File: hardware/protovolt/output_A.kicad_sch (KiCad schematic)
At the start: 46 parts, among them Q1 BSC028N06LS3, Q3 BSC028N06LS3, Q4 BSC028N06LS3, Q5 BSC028N06LS3, Q6 BSC028N06LS3, U2 LM51772RHAR

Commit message: finish demo schematic
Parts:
- removed NT1: NetTie_2, symbol Device:NetTie_2
- added C11: 100n 100V, Resistor_SMD:R_0603_1608Metric, symbol Device:C
- added C14, C16: 100n, Capacitor_SMD:C_0603_1608Metric, symbol Device:C
- added C18, C23: 680p, Capacitor_SMD:C_0603_1608Metric, symbol Device:C
- added D1: 15V, Diode_SMD:D_SOD-123, symbol Device:D_Zener
- added J1, J2, J3, J4, J5, J6, J7, J8: Conn_01x03, Connector_PinHeader_2.54mm:PinHeader_1x03_P2.54mm_Vertical_SMD_Pin1Left, symbol Connector_Generic:Conn_01x03
- added J10, J9: Conn_02x03_Odd_Even, Connector_PinHeader_2.54mm:PinHeader_2x03_P2.54mm_Vertical_SMD, symbol Connector_Generic:Conn_02x03_Odd_Even
- added R10, R14: 10R, Resistor_SMD:R_0402_1005Metric, symbol Device:R
- added R11, R12, R8: 6.98k, Resistor_SMD:R_0402_1005Metric, symbol Device:R
- added R15, R16, R17, R18, R19, R20: 3R, Resistor_SMD:R_0402_1005Metric, symbol Device:R
- added R22, R7: 0R, Resistor_SMD:R_0402_1005Metric, symbol Device:R
- added R4: 100R, Resistor_SMD:R_0402_1005Metric, symbol Device:R
- added U1: INA226, Package_SO:VSSOP-10_3x3mm_P0.5mm, symbol Sensor_Energy:INA226
- C1: renamed from C22; value 10u -> 10u 100V; footprint (none) -> Capacitor_SMD:C_1210_3225Metric; LCSC (none) -> C5156756
- C10: renamed from C24; value 39u -> 39u 50V; footprint (none) -> Capacitor_SMD:CP_Elec_8x11.9; LCSC (none) -> C193240
- C12: renamed from C6; value 0.1u -> 100n 100V; footprint (none) -> Resistor_SMD:R_0603_1608Metric; LCSC (none) -> C88219
- C13: renamed from C5; value 100n -> 100n 100V; footprint (none) -> Resistor_SMD:R_0603_1608Metric; LCSC (none) -> C88219
- C15: renamed from C3; footprint (none) -> Capacitor_SMD:C_0603_1608Metric; LCSC (none) -> C30926
- C17: renamed from C20; footprint (none) -> Capacitor_SMD:C_0603_1608Metric; LCSC (none) -> C30926
- C19: renamed from C18; footprint (none) -> Capacitor_SMD:C_0603_1608Metric; LCSC (none) -> C84419
- C2: renamed from C7; value 10u -> 10u 100V; footprint (none) -> Capacitor_SMD:C_1210_3225Metric; LCSC (none) -> C5156756
- C20: renamed from C19; footprint (none) -> Capacitor_SMD:C_0603_1608Metric; LCSC (none) -> C84419
- C21: renamed from C1; value 0.1u -> 100n 100V; footprint (none) -> Resistor_SMD:R_0603_1608Metric; LCSC (none) -> C88219
- C22: renamed from C21; footprint (none) -> Capacitor_SMD:C_0603_1608Metric; LCSC (none) -> C30926
- C24: renamed from C4; footprint (none) -> Capacitor_SMD:C_0402_1005Metric; LCSC (none) -> C440165
- C25: renamed from C2; footprint (none) -> Capacitor_SMD:C_0402_1005Metric; LCSC (none) -> C1546
- C26: renamed from C13; footprint (none) -> Capacitor_SMD:C_0402_1005Metric; LCSC (none) -> C1572
- C27: renamed from C14; footprint (none) -> Capacitor_SMD:C_0402_1005Metric; LCSC (none) -> C354977
- C28: renamed from C15; footprint (none) -> Capacitor_SMD:C_0402_1005Metric; LCSC (none) -> C1567
- C29: renamed from C16; footprint (none) -> Capacitor_SMD:C_0402_1005Metric; LCSC (none) -> C82219
- C3: renamed from C9; value 10u -> 10u 100V; footprint (none) -> Capacitor_SMD:C_1210_3225Metric; LCSC (none) -> C5156756
- C4: renamed from C12; value 10u -> 10u 100V; footprint (none) -> Capacitor_SMD:C_1210_3225Metric; LCSC (none) -> C5156756
- C5: renamed from C23; value 10u -> 10u 100V; footprint (none) -> Capacitor_SMD:C_1210_3225Metric; LCSC (none) -> C5156756
- C6: renamed from C17; value 39u -> 39u 50V; footprint (none) -> Capacitor_SMD:CP_Elec_8x11.9; LCSC (none) -> C193240
- C7: renamed from C8; value 10u -> 10u 100V; footprint (none) -> Capacitor_SMD:C_1210_3225Metric; LCSC (none) -> C5156756
- C8: renamed from C11; value 10u -> 10u 100V; footprint (none) -> Capacitor_SMD:C_1210_3225Metric; LCSC (none) -> C5156756
- C9: renamed from C10; value 39u -> 39u 50V; footprint (none) -> Capacitor_SMD:CP_Elec_8x11.9; LCSC (none) -> C193240
- L1: footprint (none) -> Inductor_SMD:L_Changjiang_FXL1050; LCSC C149528 -> C5359259
- Q1: renamed from Q6; value BSC028N06LS3 -> BSC0702LS; LCSC C534316 -> C501503
- Q2: renamed from Q1; value BSC028N06LS3 -> BSC0702LS; LCSC C534316 -> C501503
- Q3: renamed from Q4; value BSC028N06LS3 -> BSC0702LS; LCSC C534316 -> C501503
- Q4: renamed from Q3; value BSC028N06LS3 -> BSC0702LS; LCSC C534316 -> C501503
- Q5: value BSC028N06LS3 -> BSC0702LS; LCSC C534316 -> C501503
- R1: renamed from R4; value R -> 0.010R; footprint (none) -> Resistor_SMD:R_2512_6332Metric; LCSC (none) -> C393070
- R13: renamed from R8; footprint (none) -> Resistor_SMD:R_0402_1005Metric; LCSC (none) -> C21376
- R2: footprint (none) -> Resistor_SMD:R_0402_1005Metric; LCSC (none) -> C286566
- R21: renamed from R9; footprint (none) -> Resistor_SMD:R_0402_1005Metric; LCSC (none) -> C25139
- R23: renamed from R10; footprint (none) -> Resistor_SMD:R_0402_1005Metric; LCSC (none) -> C25139
- R24: renamed from R11; footprint (none) -> Resistor_SMD:R_0402_1005Metric; LCSC (none) -> C47500
- R25: renamed from R16; footprint (none) -> Resistor_SMD:R_0402_1005Metric; LCSC (none) -> C25893
- R26: renamed from R20; value 20.5k -> 2.7k; footprint (none) -> Resistor_SMD:R_0402_1005Metric; LCSC (none) -> C25885
- R27: renamed from R21; footprint (none) -> Resistor_SMD:R_0402_1005Metric; LCSC (none) -> C21376
- R28: renamed from R22; value 33k -> 30.9k; footprint (none) -> Resistor_SMD:R_0402_1005Metric; LCSC C25555 -> C310222
- R3: renamed from R1; footprint (none) -> Resistor_SMD:R_2512_6332Metric; LCSC (none) -> C5375459
- R5: renamed from R3; value 511R -> 30.9k; footprint (none) -> Resistor_SMD:R_0402_1005Metric; LCSC (none) -> C310222
- R6: value 100k -> 0R; footprint (none) -> Resistor_SMD:R_0402_1005Metric; LCSC (none) -> C21376
- R9: renamed from R7; footprint (none) -> Resistor_SMD:R_0402_1005Metric; LCSC (none) -> C21376
- U2: LCSC (none) -> C41383743
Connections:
- net CSA: now also C18.1
- net DRV: now also R4.2; no longer Q1.4 (G)
- net GND: now also C12.1, C13.2, C19.2, C21.1, C25.2, C26.2, C27.2, C28.2, C29.2, R25.2, R26.2, R27.2, R28.2, U2.17 (AGND), U2.41 (GND), C11.1, C14.2, J10.1 (Pin_1), J10.3 (Pin_3), J10.5 (Pin_5), J3.3 (Pin_3), J5.3 (Pin_3), J6.3 (Pin_3), J7.3 (Pin_3), J8.3 (Pin_3), J9.2 (Pin_2), J9.4 (Pin_4), J9.6 (Pin_6), R16.2, R19.2, R7.1, U1.7 (GND)
- net HO1: now also R15.2; no longer U2.24 (HO1)
- net HO2: now also R18.2; no longer U2.32 (HO2)
- net ISNSN: now also R14.2
- net ISNSP: now also R10.2
- net LO1: now also R17.2; no longer U2.27 (LO1)
- net LO2: now also R20.2; no longer U2.30 (LO2)
- net SW2: now also C23.1
- net VBUS: now reaches C1.1, C12.2, C6.1, Q2.5 (D), R2.1, U2.36 (VIN)
- net VBUS: now also J10.2 (Pin_2), J10.4 (Pin_4), J10.6 (Pin_6), J2.1 (Pin_1), J8.1 (Pin_1)
- net at R6.2: now also U2.14 (FB/INT); no longer U2.11 (FLT)
- net VCC2: now reaches C20.1, R6.1, U2.29 (VCC2)
- net VCC2: now also J3.1 (Pin_1), J5.1 (Pin_1); no longer U2.14 (FB/INT), U2.7 (MODE)
- net ATRK: now reaches C29.1, U2.2 (SS/ATRK)
- net ATRK: now also J7.2 (Pin_2)
- net SYNC: now reaches U2.3 (SYNC)
- net SYNC: now also J5.2 (Pin_2)
- net at R2.2, R5.1, U2.37 (EN/UVLO): now also C11.2
- net RST: now reaches U2.38 (RST)
- net RST: now also J8.2 (Pin_2)
- net DTRK: now reaches U2.4 (DTRK)
- net DTRK: now also J7.1 (Pin_1)
- net BIAS: now reaches C21.2, U2.40 (BIAS)
- net BIAS: now also J2.2 (Pin_2), R22.1
- net SDA: now reaches U2.5 (CFG3(SDA))
- net SDA: now also J6.2 (Pin_2)
- net SCL: now reaches U2.6 (CFG4(SCL))
- net SCL: now also J6.1 (Pin_1)
- net at C10.1, C5.1, Q1.1 (S)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: now also D1.2 (A), J9.1 (Pin_1), J9.3 (Pin_3), J9.5 (Pin_5), U1.8 (Vbus)
- removed net GNDA: C12.1, C13.2, C19.2, C21.1, C25.2, C26.2, C27.2, C28.2, C29.2, R25.2, R26.2, R27.2, R28.2, U2.15 (VIN-FB), U2.17 (AGND), U2.41 (GND)
- new net: J4.2 (Pin_2), R11.2, U1.5 (SCL)
- new net: J4.1 (Pin_1), R12.2, U1.3 (~{Alert})
- new net: C16.1, R10.1, U1.10 (Vin+)
- new net: C16.2, R14.1, U1.9 (Vin-)
- new net: D1.1 (K), Q1.4 (G), R4.1
- new net: R15.1, U2.24 (HO1)
- new net: R7.2, U2.15 (VIN-FB)
- new net: R17.1, U2.27 (LO1)
- new net: R20.1, U2.30 (LO2)
- new net: R18.1, U2.32 (HO2)
- new net: C23.2, R19.1
- new net: J1.1 (Pin_1), U1.2 (A0)
- new net: J1.2 (Pin_2), U1.1 (A1)
- new net: C18.2, R16.1
- new net: J4.3 (Pin_3), R8.2, U1.4 (SDA)
- new net +3V3: C14.1, J1.3 (Pin_3), R11.1, R12.1, R8.1, U1.6 (VS)
- new net FLT: R22.2, U2.11 (FLT)
- new net MODE: J3.2 (Pin_2), U2.7 (MODE)
- no-connect marks 0 -> 1
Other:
- note added: "+5V: PWM/CCM GND: SLEEP"
- note added: "BSC0702LS 60V 84A 83W 2.7mΩ@10V,50A 2.3V 1 N-channel TDSON-8-EP(5x6) MOSFETs ROHS BSC028N06LS3 60V 100A 2.8mΩ@10V,50A 139W 2.2V 1 N-channel TDSON-8(5.2x5.9) MOSFETs ROHS"
- note added: "RT to GND I2C ADDR 0x6A RT to VCC2 I2C ADDR 0x6B"
- note added: "SOFT START 4.7ms"
- note added: "UVLO - RISING 4.28V - FALLING 4.11V"
- moved on the sheet: C15, C17, C22, C24, Q1, R13, R21, R23, R9

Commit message: route h-bridge
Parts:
- R22: value 0R -> 6.98k
- R3: LCSC C5375459 -> C20539438
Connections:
- net BIAS: no longer R22.1
- net VCC2: now also R22.1
- net ISNS_N: now reaches C15.1, R13.1, U2.19 (ISNSN)
- net ISNS_P: now reaches C15.2, R9.1, U2.20 (ISNSP)
- net CS_N: now reaches C24.2, R23.1, U2.21 (CSB)
- net CS_P: now reaches C24.1, R21.1, U2.22 (CSA)
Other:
- note added: "BSC0702LS 60V 84A 83W 2.7mΩ@10V,50A 2.3V 1 N-channel TDSON-8-EP(5x6) MOSFETs ROHS BSC028N06LS3 60V 100A 2.8mΩ@10V,50A 139W 2.2V 1 N-channel TDSON-8(5.2x5.9) MOSFETs ROHS IAUC60N04S6L030HATMA HALF-BRIDGE"
- note removed: "BSC0702LS 60V 84A 83W 2.7mΩ@10V,50A 2.3V 1 N-channel TDSON-8-EP(5x6) MOSFETs ROHS BSC028N06LS3 60V 100A 2.8mΩ@10V,50A 139W 2.2V 1 N-channel TDSON-8(5.2x5.9) MOSFETs ROHS"
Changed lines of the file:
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@@
 	)
 	(junction
+		(at 129.54 163.83)
+		(diameter 0)
+		(color 0 0 0 0)
+	)
+	(junction
 		(at 212.09 173.99)
 		(diameter 0)
@@
 	)
 	(junction
-		(at 129.54 168.91)
-		(diameter 0)
-		(color 0 0 0 0)
-	)
-	(junction
 		(at 152.4 163.83)
 		(diameter 0)
@@
 	(wire
 		(pts
-			(xy 129.54 168.91) (xy 154.94 168.91)
+			(xy 110.49 168.91) (xy 154.94 168.91)
 		)
 		(stroke
@@
 	(wire
 		(pts
-			(xy 105.41 163.83) (xy 152.4 163.83)
+			(xy 105.41 163.83) (xy 129.54 163.83)
 		)
 		(stroke
@@
 	(wire
 		(pts
+			(xy 129.54 163.83) (xy 152.4 163.83)
+		)
+		(stroke
+			(width 0)
+			(type default)
+		)
+	)
+	(wire
+		(pts
 			(xy 195.58 176.53) (xy 200.66 176.53)
 		)
@@
 	(wire
 		(pts
-			(xy 129.54 195.58) (xy 129.54 168.91)
-		)
-		(stroke
-			(width 0)
-			(type default)
-		)
-	)
-	(wire
-		(pts
 			(xy 144.78 203.2) (xy 154.94 203.2)
 		)
@@
 	(wire
 		(pts
+			(xy 129.54 163.83) (xy 129.54 195.58)
+		)
+		(stroke
+			(width 0)
+			(type default)
+		)
+	)
+	(wire
+		(pts
 			(xy 320.04 151.13) (xy 322.58 151.13)
 		)
@@
 		)
 	)
-	(wire
-		(pts
-			(xy 110.49 168.91) (xy 129.54 168.91)
-		)
-		(stroke
-			(width 0)
-			(type default)
-		)
-	)
 	(text "UVLO\n- RISING 4.28V\n- FALLING 4.11V"
 		(exclude_from_sim no)
@@
 		)
 	)
-	(text "BSC0702LS\n60V 84A 83W 2.7mΩ@10V,50A 2.3V 1 N-channel TDSON-8-EP(5x6) MOSFETs ROHS\n\nBSC028N06LS3\n60V 100A 2.8mΩ@10V,50A 139W 2.2V 1 N-channel TDSON-8(5.2x5.9) MOSFETs ROHS\n"
+	(text "BSC0702LS\n60V 84A 83W 2.7mΩ@10V,50A 2.3V 1 N-channel TDSON-8-EP(5x6) MOSFETs ROHS\n\nBSC028N06LS3\n60V 100A 2.8mΩ@10V,50A 139W 2.2V 1 N-channel TDSON-8(5.2x5.9) MOSFETs ROHS\n\nIAUC60N04S6L030HATMA\nHALF-BRIDGE"
 		(exclude_from_sim no)
 		(at 138.684 53.34 0)
@@
 		)
 	)
+	(label "CS_P"
+		(at 196.85 193.04 0)
+		(fields_autoplaced yes)
+		(effects
+			(font
+				(size 1.27 1.27)
+			)
+			(justify left bottom)
+		)
+	)
 	(label "SW2"
 		(at 194.31 85.09 180)
@@
 		)
 	)
+	(label "ISNS_P"
+		(at 196.85 161.29 0)
+		(fields_autoplaced yes)
+		(effects
+			(font
+				(size 1.27 1.27)
+			)
+			(justify left bottom)
+		)
+	)
 	(label "SW1"
 		(at 143.51 85.09 0)
@@
 		)
 	)
+	(label "CS_N"
+		(at 196.85 195.58 0)
+		(fields_autoplaced yes)
+		(effects
+			(font
+				(size 1.27 1.27)
+			)
+			(justify left bottom)
+		)
+	)
 	(label "MODE"
 		(at 144.78 179.07 0)
@@
 		)
 	)
+	(label "ISNS_N"
+		(at 196.85 163.83 0)
+		(fields_autoplaced yes)
+		(effects
+			(font
+				(size 1.27 1.27)
+			)
+			(justify left bottom)
+		)
+	)
 	(label "SYNC"
 		(at 144.78 181.61 0)
@@
 		(dnp no)
 		(property "Reference" "R22"
-			(at 130.81 195.326 0)
+			(at 134.366 191.262 90)
 			(effects
 				(font
 					(size 1.27 1.27)
 				)
-				(justify left)
+				(justify right)
 			)
 		)
-		(property "Value" "0R"
-			(at 133.35 195.326 0)
+		(property "Value" "6.98k"
+			(at 134.366 193.294 90)
 			(effects
 				(font
 					(size 1.27 1.27)
 				)
-				(justify left)
+				(justify right)
 			)
 		)
@@
 			)
 		)
-		(property "LCSC" "C5375459"
+		(property "LCSC" "C20539438"
 			(at 166.37 85.09 0)
 			(effects

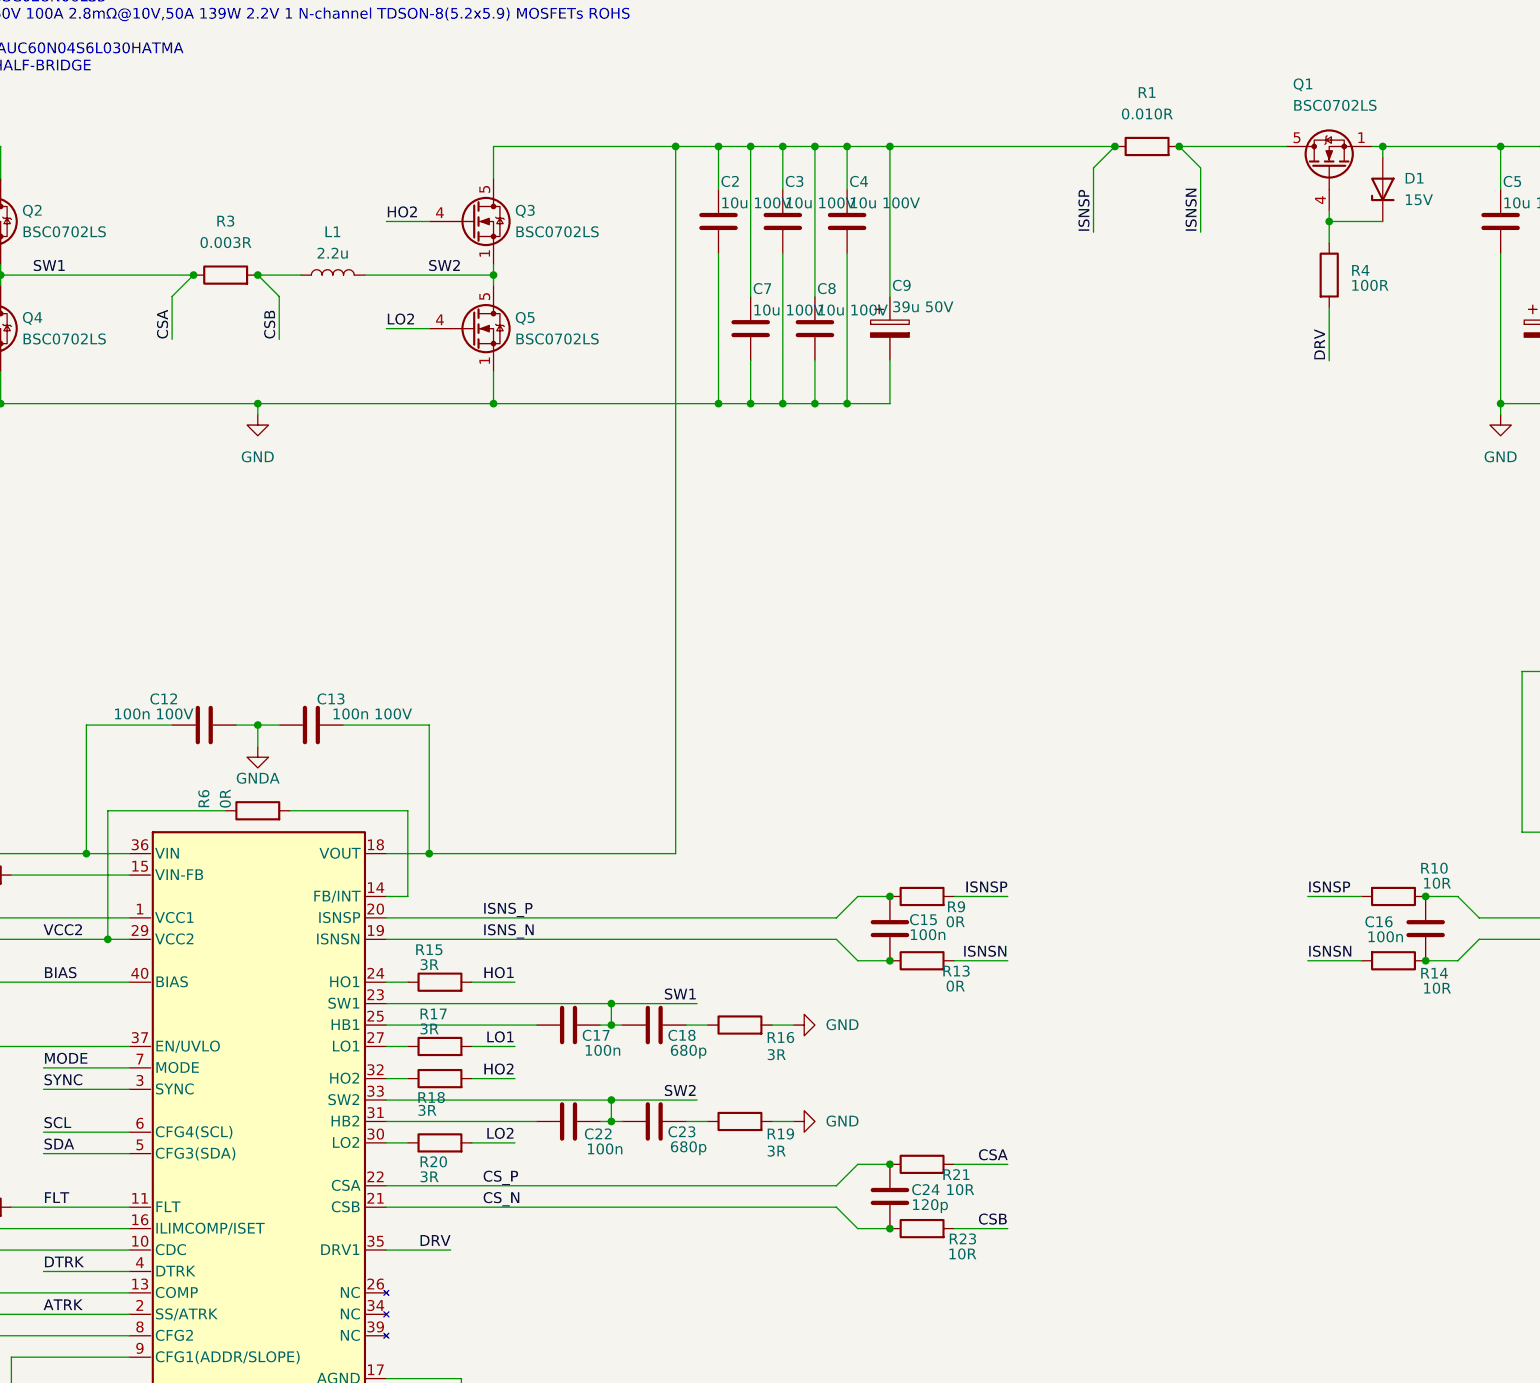
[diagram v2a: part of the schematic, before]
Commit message: fet routing
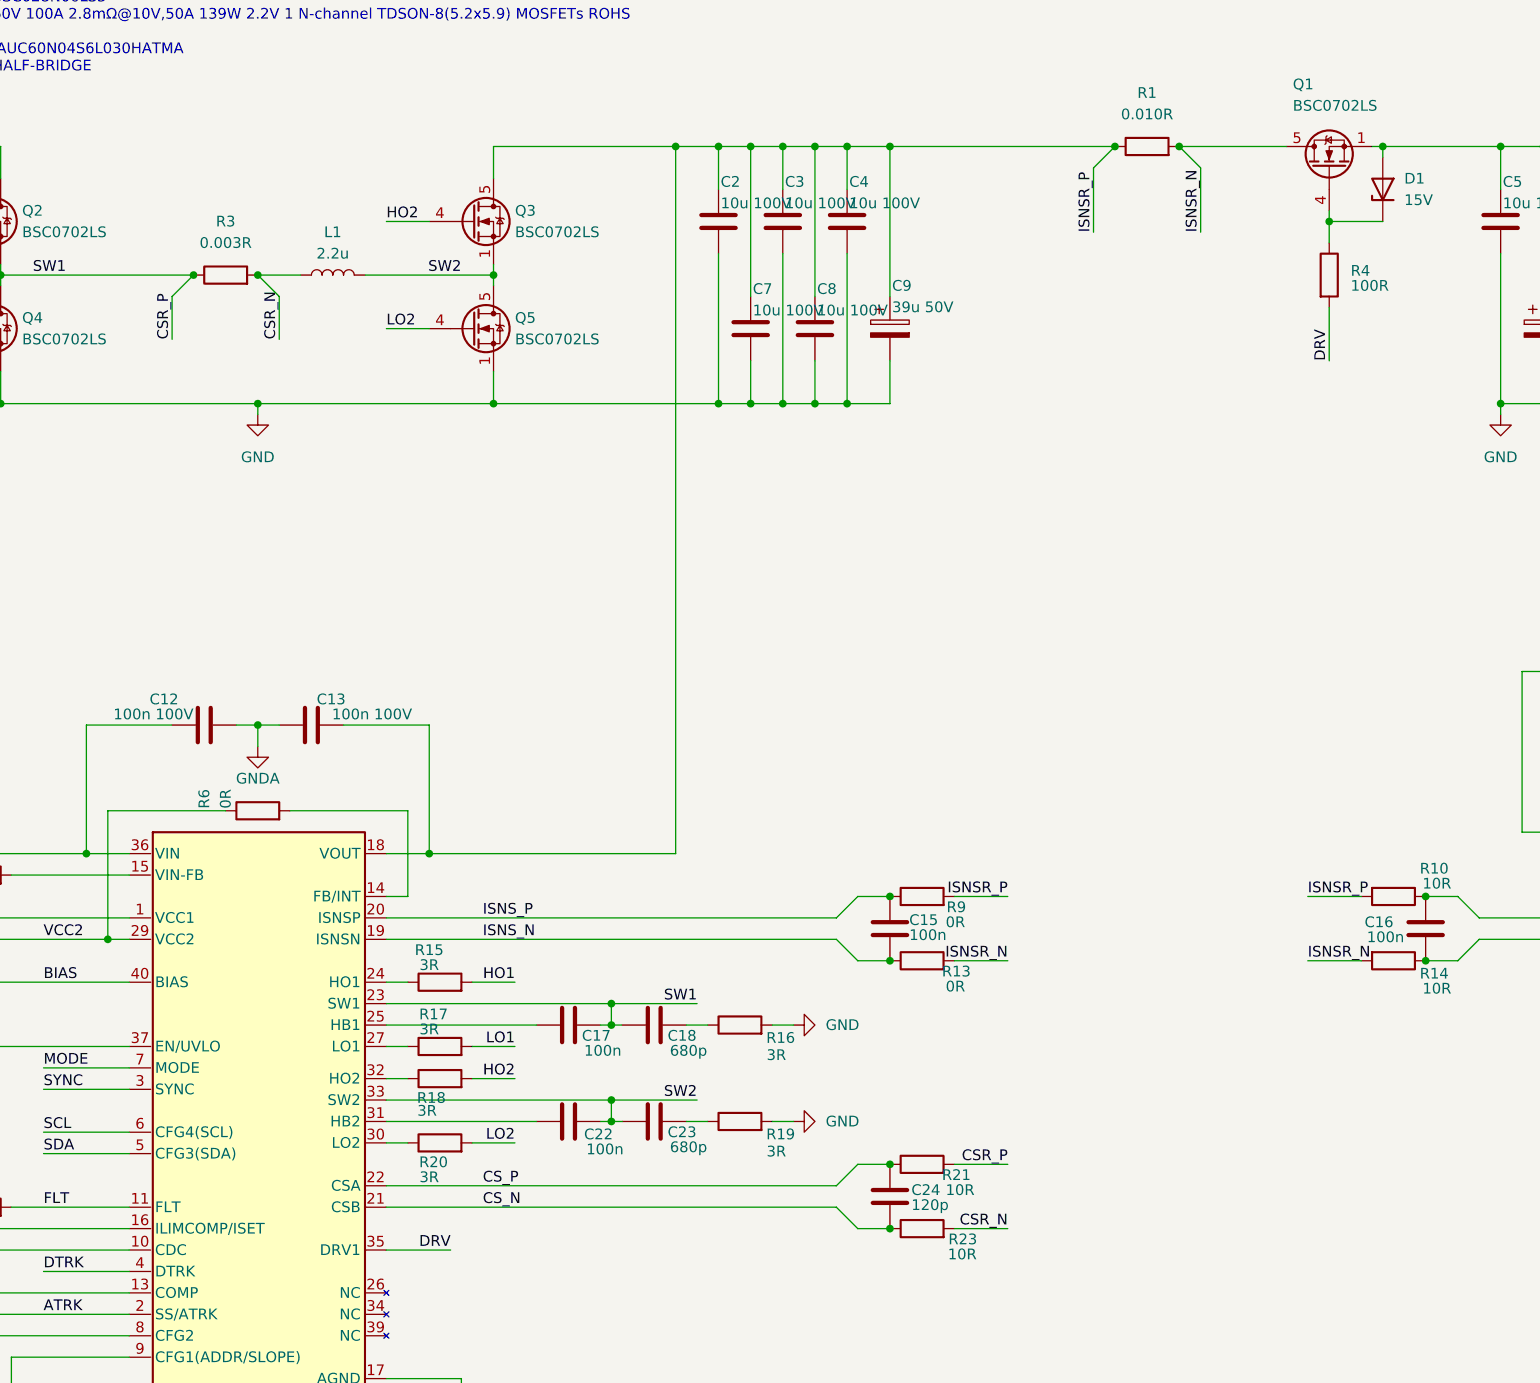
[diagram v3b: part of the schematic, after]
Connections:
- net CSA renamed CSR_P
- net CSB renamed CSR_N
- net ISNSN renamed ISNSR_N
- net ISNSP renamed ISNSR_P
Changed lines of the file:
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@@
 		)
 	)
-	(label "ISNSP"
+	(label "ISNSR_P"
 		(at 259.08 158.75 180)
 		(fields_autoplaced yes)
@@
 		)
 	)
-	(label "CSB"
+	(label "CSR_N"
 		(at 172.72 92.71 90)
 		(fields_autoplaced yes)
@@
 		)
 	)
-	(label "ISNSP"
+	(label "ISNSR_P"
 		(at 294.64 158.75 0)
 		(fields_autoplaced yes)
@@
 		)
 	)
-	(label "ISNSN"
+	(label "ISNSR_N"
 		(at 281.94 80.01 90)
 		(fields_autoplaced yes)
@@
 		)
 	)
-	(label "CSB"
+	(label "CSR_N"
 		(at 259.08 198.12 180)
 		(fields_autoplaced yes)
@@
 		)
 	)
-	(label "ISNSP"
+	(label "ISNSR_P"
 		(at 269.24 80.01 90)
 		(fields_autoplaced yes)
@@
 		)
 	)
-	(label "ISNSN"
+	(label "ISNSR_N"
 		(at 259.08 166.37 180)
 		(fields_autoplaced yes)
@@
 		)
 	)
-	(label "CSA"
+	(label "CSR_P"
 		(at 160.02 92.71 90)
 		(fields_autoplaced yes)
@@
 		)
 	)
-	(label "CSA"
+	(label "CSR_P"
 		(at 259.08 190.5 180)
 		(fields_autoplaced yes)
@@
 		)
 	)
-	(label "ISNSN"
+	(label "ISNSR_N"
 		(at 294.64 166.37 0)
 		(fields_autoplaced yes)

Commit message: four layer
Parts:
- L1: footprint Inductor_SMD:L_Changjiang_FXL1050 -> protovolt:L_Changjiang_FXL1050
- R3: footprint Resistor_SMD:R_2512_6332Metric -> Resistor_SMD:R_1206_3216Metric; LCSC C20539438 -> C326610
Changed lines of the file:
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@@
 			)
 		)
-		(property "Footprint" "Inductor_SMD:L_Changjiang_FXL1050"
+		(property "Footprint" "protovolt:L_Changjiang_FXL1050"
 			(at 179.07 85.09 0)
 			(effects
@@
 			)
 		)
-		(property "Footprint" "Resistor_SMD:R_2512_6332Metric"
+		(property "Footprint" "Resistor_SMD:R_1206_3216Metric"
 			(at 166.37 86.868 90)
 			(effects
@@
 			)
 		)
-		(property "LCSC" "C20539438"
+		(property "LCSC" "C326610 "
 			(at 166.37 85.09 0)
 			(effects

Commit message: wire all
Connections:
- net ATRK: now also J7.1 (Pin_1); no longer J7.2 (Pin_2)
- net DTRK: now also J7.2 (Pin_2); no longer J7.1 (Pin_1)
- net GND: now also J2.3 (Pin_3)
- no-connect marks 1 -> 0
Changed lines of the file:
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@@
 		(color 0 0 0 0)
 	)
-	(no_connect
-		(at 69.85 149.86)
-	)
 	(wire
 		(pts
@@
 		)
 	)
+	(label "DTRK"
+		(at 77.47 208.28 180)
+		(fields_autoplaced yes)
+		(effects
+			(font
+				(size 1.27 1.27)
+			)
+			(justify right bottom)
+		)
+	)
 	(label "ISNSR_P"
 		(at 294.64 158.75 0)
@@
 		)
 	)
-	(label "DTRK"
-		(at 77.47 205.74 180)
+	(label "SCL"
+		(at 144.78 186.69 0)
 		(fields_autoplaced yes)
 		(effects
@@
 				(size 1.27 1.27)
 			)
-			(justify right bottom)
+			(justify left bottom)
 		)
 	)
 	(label "ATRK"
-		(at 77.47 208.28 180)
+		(at 77.47 205.74 180)
 		(fields_autoplaced yes)
 		(effects
@@
 		)
 	)
-	(label "SCL"
-		(at 144.78 186.69 0)
-		(fields_autoplaced yes)
-		(effects
-			(font
-				(size 1.27 1.27)
-			)
-			(justify left bottom)
-		)
-	)
 	(label "VCC2"
 		(at 144.78 163.83 0)
@@
 					(unit 1)
 				)
+			)
+		)
+	)
+	(symbol
+		(lib_id "power:GNDA")
+		(at 69.85 149.86 0)
+		(unit 1)
+		(exclude_from_sim no)
+		(in_bom yes)
+		(on_board yes)
+		(dnp no)
+		(fields_autoplaced yes)
+		(property "Reference" "#PWR028"
+			(at 69.85 156.21 0)
+			(effects
+				(font
+					(size 1.27 1.27)
+				)
+				(hide yes)
+			)
+		)
+		(property "Value" "GNDA"
+			(at 69.85 154.94 0)
+			(effects
+				(font
+					(size 1.27 1.27)
+				)
+			)
+		)
+		(property "Footprint" ""
+			(at 69.85 149.86 0)
+			(effects
+				(font
+					(size 1.27 1.27)
+				)
+				(hide yes)
+			)
+		)
+		(property "Datasheet" ""
+			(at 69.85 149.86 0)
+			(effects
+				(font
+					(size 1.27 1.27)
+				)
+				(hide yes)
+			)
+		)
+		(property "Description" "Power symbol creates a global label with name \"GNDA\" , analog ground"
+			(at 69.85 149.86 0)
+			(effects
+				(font
+					(size 1.27 1.27)
+				)
+				(hide yes)
+			)
+		)
+		(pin "1"
+		)
+		(instances
+			(project "protovolt"
+				(path "/ea7037dc-92a2-412b-b904-472cbab72219/4a270319-7ef6-4bc5-85c2-eebc7d78bfc0"
+					(reference "#PWR028")
+					(unit 1)
+				)
